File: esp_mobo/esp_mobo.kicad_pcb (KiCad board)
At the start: 2 copper layers, 75.5 x 71 mm, 77 parts, among them J10 Conn_01x03_Pin, J11 Conn_01x03_Pin, J12 Conn_01x03_Pin, J13 Conn_01x03_Pin, J14 Conn_01x03_Pin, J15 Conn_01x03_Pin, J16 Screw_Terminal_01x02, J17 Conn_01x03_Pin, J2 Screw_Terminal_01x02, J3 Conn_01x03_Pin, J5 Conn_01x03_Pin, J6 Conn_01x03_Pin, J7 Conn_01x03_Pin, J8 Conn_01x03_Pin, J9 Conn_01x03_Pin, U1 ESP32-DevKitC, U2 74AHCT125, U3 PC847, U4 PC847, U5 BME280, U6 TMCS1100A2QDR, U7 LM4030-2.5, U8 TMCS1100A2QDR, U9 LM4030-2.5

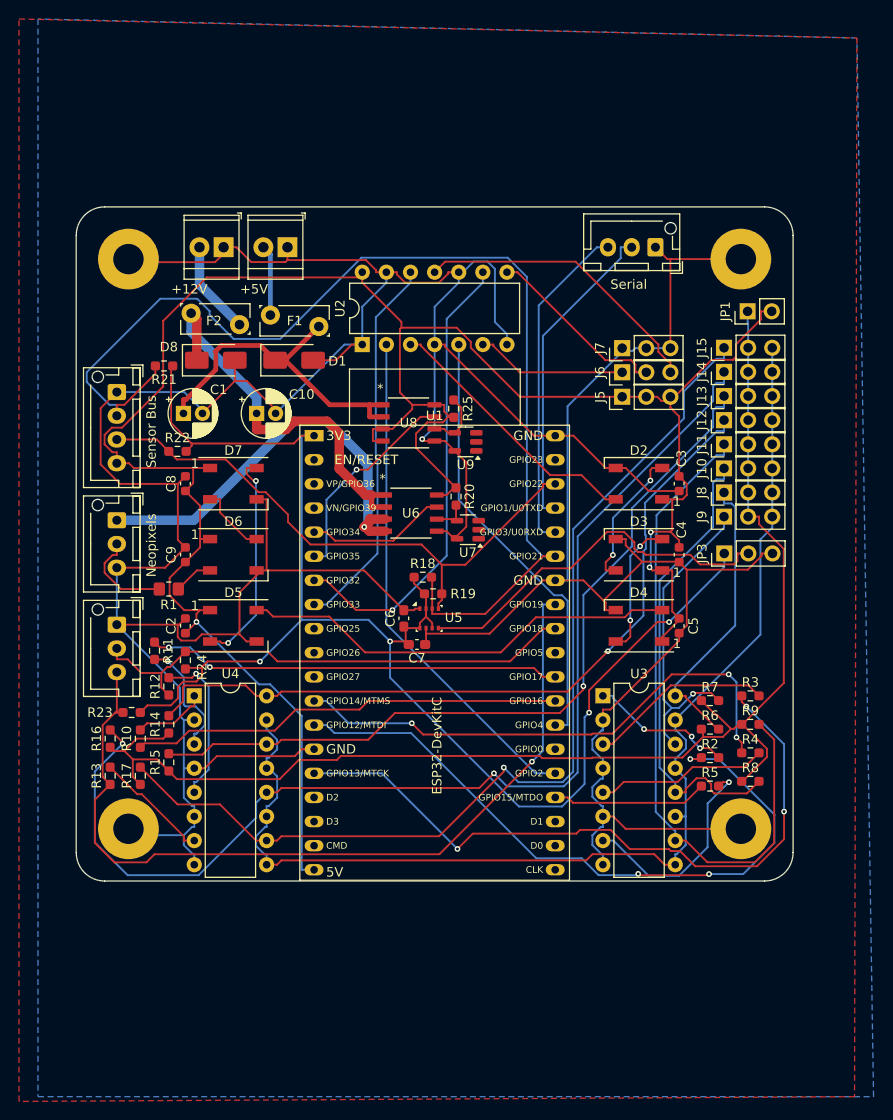
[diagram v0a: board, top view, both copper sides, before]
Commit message: Add leak sensor
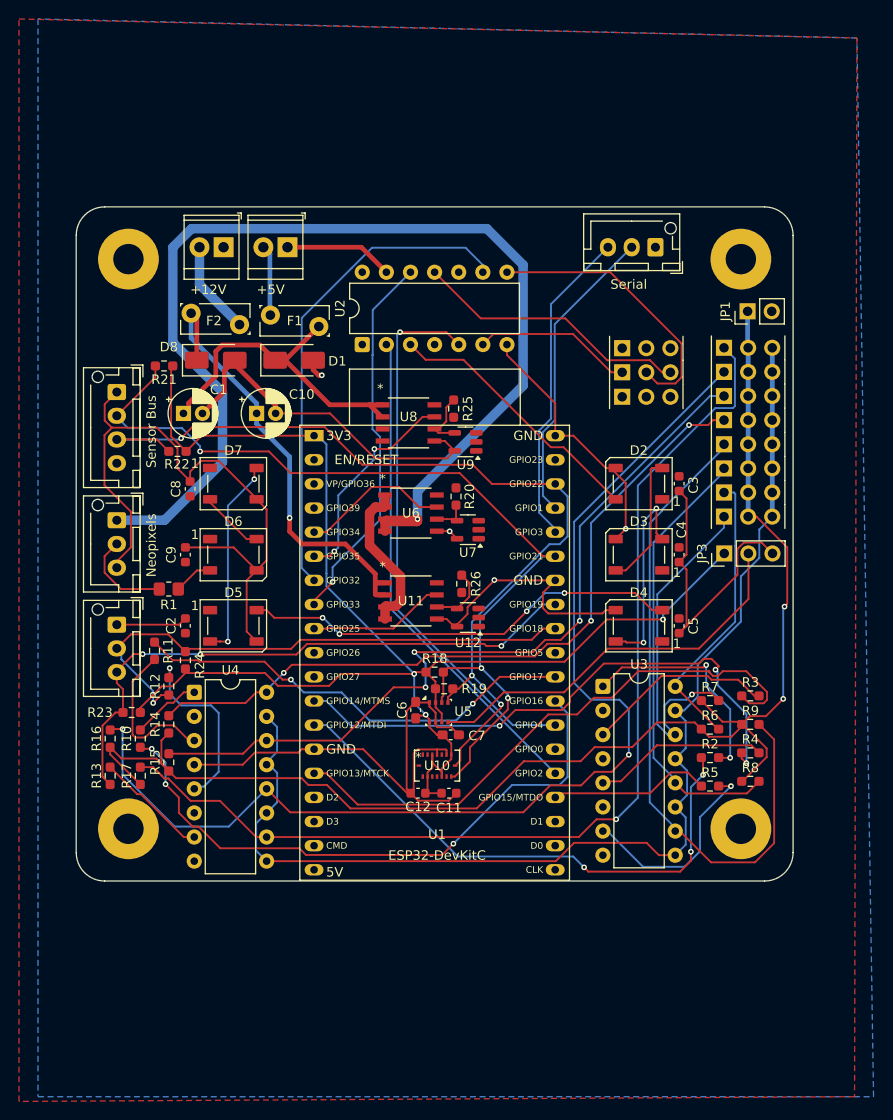
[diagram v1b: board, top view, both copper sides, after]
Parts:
- added C11: 0.1uF, Capacitor_SMD:C_0603_1608Metric, F.Cu at (147.2, 132.2)
- added C12: 0.1uF, Capacitor_SMD:C_0603_1608Metric, F.Cu at (144.0, 132.2)
- added R26: 20K, Resistor_SMD:R_0603_1608Metric_Pad0.98x0.95mm_HandSolder, F.Cu at (148.6, 110.2)
- added U10: BMI088, BMI088:QFN_BMI085_BOS, F.Cu at (146.0, 129.3)
- added U11: TMCS1100A2QDR, TMCS1100:SOIC8_D_TEX, F.Cu at (143.2, 112.0)
- added U12: LM4030-2.5, Package_TO_SOT_SMD:SOT-23-5, F.Cu at (149.2, 113.8)
- J10, J11, J12, J13, J14, J15, J5, J6, J7, J8, J9: footprint Connector_PinHeader_2.54mm:PinHeader_1x03_P2.54mm_Vertical -> ConnectorSmallCourtyard:PinHeader_1x03_P2.54mm_Vertical_small_courtyard
- U6, U8: footprint TMCS1100A2QDR:SOIC8_D_TEX -> TMCS1100:SOIC8_D_TEX
- moved C7 10.2 mm to (147.4, 126.1)
- moved R18 10.1 mm to (145.8, 119.5)
- moved R19 10.1 mm to (146.8, 121.2)
- moved U5 9.94 mm to (146.2, 123.7)
- moved C6 9.74 mm to (143.8, 123.5)
- moved U3 1.00 mm to (163.5, 121.0)
- moved C8 0.74 mm to (120.0, 100.2)
- moved U4 0.38 mm to (120.4, 121.6)
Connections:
- C10 pad 1: NeoPowerIn -> 12VInput
- D8 pad 1: NeoPowerIn -> 12VInput
- F2 pad 2: NeoPowerIn -> 12VInput
- H1 pad 1: GND -> unconnected-(H1-Pad1)
- H2 pad 1: GND -> unconnected-(H2-Pad1)
- H3 pad 1: GND -> unconnected-(H3-Pad1)
- H4 pad 1: GND -> unconnected-(H4-Pad1)
- U1 pad 9: unconnected-(U1-DAC_1/ADC2_CH8/GPIO25-Pad9) -> CurrentSens12V
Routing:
- net +5V: track 236.7 -> 0.34 mm, vias 3 -> 0
- net GND: track 473.4 -> 275.5 mm, vias 1 -> 4
- net NeoPowerOut: track 44.6 -> 121.0 mm
- net 12VInput: track 0.00 -> 47.6 mm, vias 0 -> 1
- net SCL: track 60.6 -> 97.7 mm, vias 0 -> 3
- net Motor 8 Signal: track 89.9 -> 63.2 mm, vias 1 -> 3
- net NeoPowerIn: track 42.3 -> 17.2 mm
- net SDA: track 120.5 -> 98.7 mm, vias 0 -> 3
- net Motor 5 Signal: track 45.7 -> 63.9 mm, vias 0 -> 3
- net CurrentSens12V: track 0.00 -> 14.4 mm
- net Motor 1 Signal: track 72.1 -> 58.0 mm
- net Motor 2 Signal: track 73.3 -> 60.2 mm, vias 3 -> 0
- net Servo1 Data In: track 46.6 -> 57.7 mm, vias 0 -> 1
- net Servo2 Data Out: track 19.5 -> 29.5 mm
- net Net-(R2-Pad2): track 15.2 -> 23.9 mm, vias 3 -> 2
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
